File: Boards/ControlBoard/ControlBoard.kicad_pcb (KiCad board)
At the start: 4 copper layers, 250 x 150 mm, 181 parts, among them IC1 TXB0104DR, IC2 ADS8688AIDBT, IC3 ISO1042BDWVR, IC4 TXB0104DR, IC5 TXB0104DR, IC6 MCP2515-e_ST, IC7 TXB0104DR, IC8 TXB0104DR, J1 Conn_01x02_Pin, J10 5-106505-2, J11 5-106505-2, J12 5-106505-2, J13 5-106505-2, J14 5-106505-2, J15 1987724, J16 1987724, J17 1548129, J24 5442251, J3 1548129, J4 5-106505-2, J5 5442251, J6 L717SDB25PA4CH3R, J7 5442251, J8 5442251, J9 5442251, M1 Fan_4pin, M2 Fan_4pin, M3 Fan_4pin, M4 Fan_4pin, M5 Fan_4pin, M6 Fan_4pin, M7 Fan_4pin, M8 Fan_4pin, Y1 8MHz

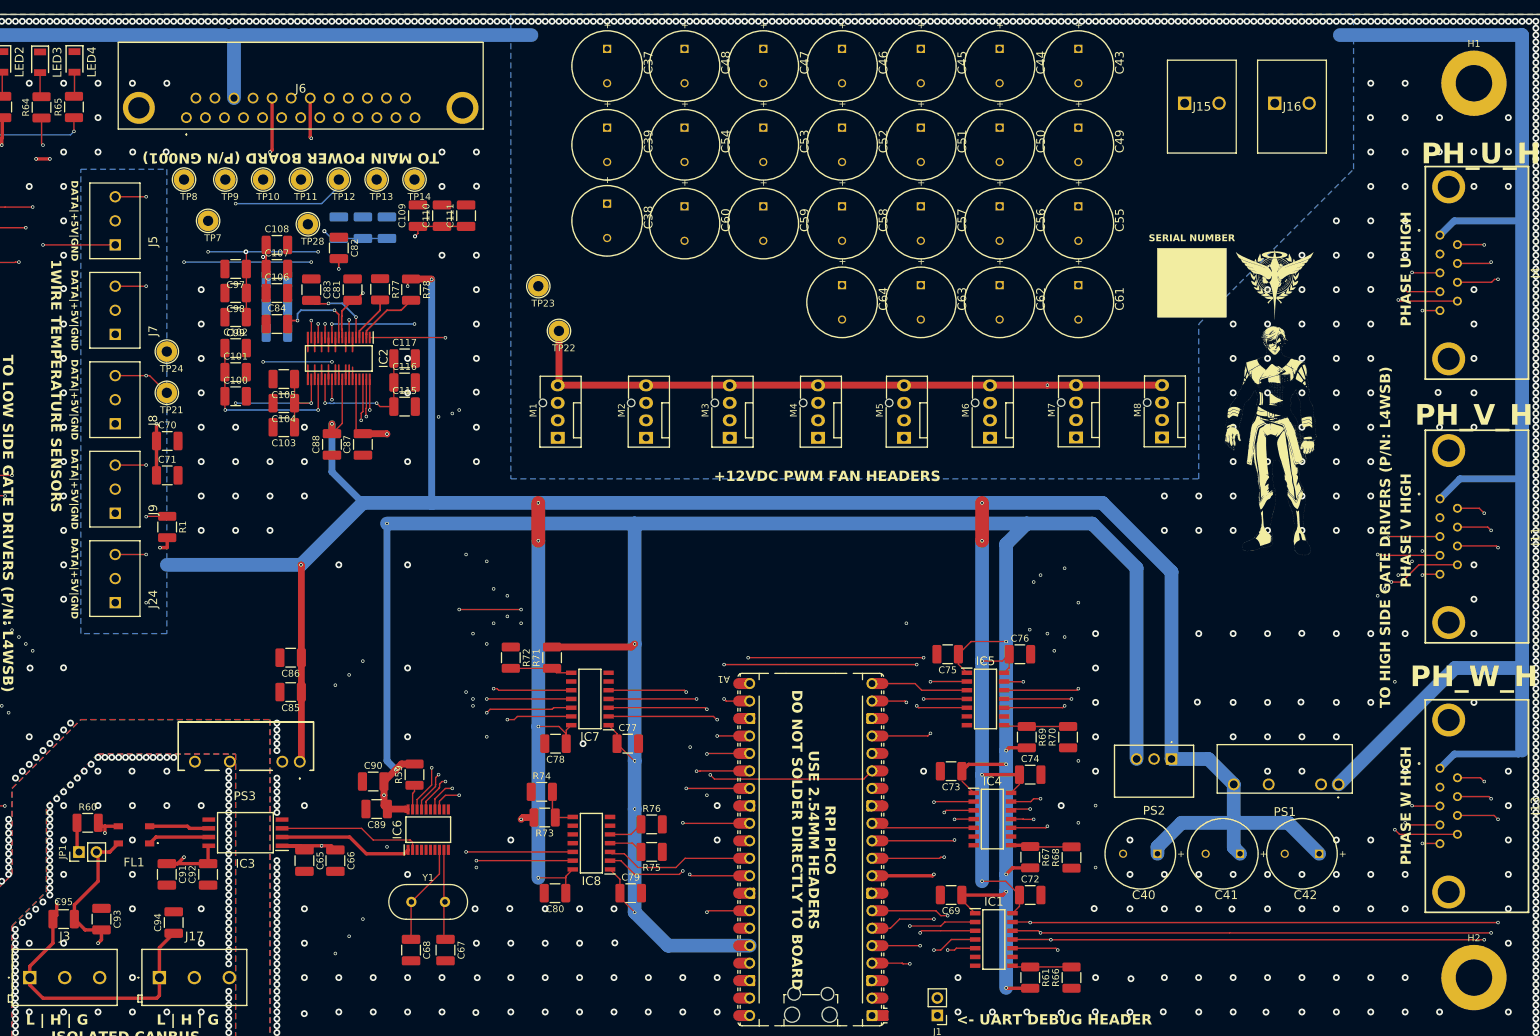
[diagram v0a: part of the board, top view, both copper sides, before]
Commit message: Update control board
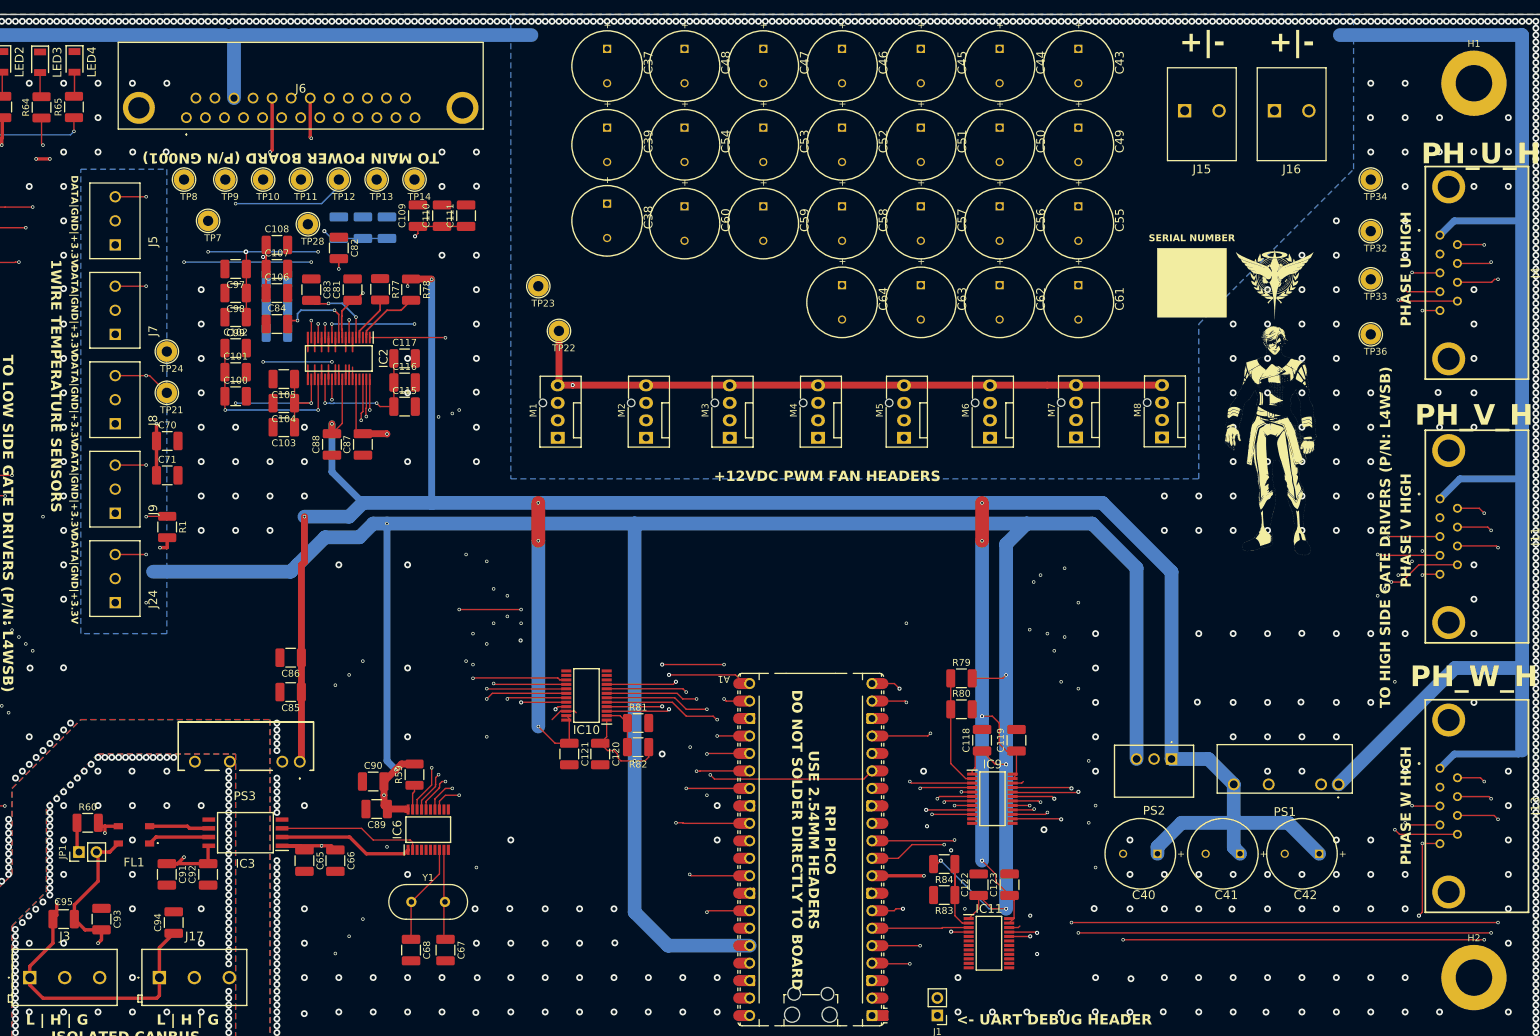
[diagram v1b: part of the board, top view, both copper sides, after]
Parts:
- removed C69, C72, C73, C74, C75, C76, C77, C78, C79, C80: 100nF, Capacitor_SMD:C_1210_3225Metric_Pad1.33x2.70mm_HandSolder
- removed IC1, IC4, IC5, IC7, IC8: TXB0104DR, InverterCom:SOIC127P600X175-14N
- removed R61, R66, R67, R68, R69, R70, R71, R72, R73, R74, R75, R76: 4.7k, Resistor_SMD:R_1210_3225Metric_Pad1.30x2.65mm_HandSolder
- removed REF**: OSHW-Logo2_14.6x12mm_SilkScreen, Symbol:OSHW-Logo2_14.6x12mm_SilkScreen
- removed REF**: ESD-Logo_13.2x12mm_SilkScreen, Symbol:ESD-Logo_13.2x12mm_SilkScreen
- removed REF**: KiCad-Logo2_8mm_SilkScreen, Symbol:KiCad-Logo2_8mm_SilkScreen
- removed REF**: WEEE-Logo_8.4x12mm_SilkScreen, Symbol:WEEE-Logo_8.4x12mm_SilkScreen
- added C118: 100nF, Capacitor_SMD:C_1210_3225Metric_Pad1.33x2.70mm_HandSolder, F.Cu at (193.5, 130.5)
- added C119: 100nF, Capacitor_SMD:C_1210_3225Metric_Pad1.33x2.70mm_HandSolder, F.Cu at (198.5, 130.5)
- added C120: 100nF, Capacitor_SMD:C_1210_3225Metric_Pad1.33x2.70mm_HandSolder, F.Cu at (138.0, 132.5)
- added C121: 100nF, Capacitor_SMD:C_1210_3225Metric_Pad1.33x2.70mm_HandSolder, F.Cu at (133.5, 132.5)
- added C122: 100nF, Capacitor_SMD:C_1210_3225Metric_Pad1.33x2.70mm_HandSolder, F.Cu at (193.0, 151.5)
- added C123: 100nF, Capacitor_SMD:C_1210_3225Metric_Pad1.33x2.70mm_HandSolder, F.Cu at (197.5, 151.5)
- added IC10: SN74LXCH8T245PWR, InverterCom:SOP65P640X120-24N, F.Cu at (136.0, 124.0)
- added IC11: SN74LXCH8T245PWR, InverterCom:SOP65P640X120-24N, F.Cu at (194.5, 160.0)
- added IC9: SN74LXCH8T245PWR, InverterCom:SOP65P640X120-24N, F.Cu at (195.0, 139.0)
- added R79: 4.7k, Resistor_SMD:R_1210_3225Metric_Pad1.30x2.65mm_HandSolder, F.Cu at (190.5, 121.5)
- added R80: 4.7k, Resistor_SMD:R_1210_3225Metric_Pad1.30x2.65mm_HandSolder, F.Cu at (190.5, 126.0)
- added R81: 4.7k, Resistor_SMD:R_1210_3225Metric_Pad1.30x2.65mm_HandSolder, F.Cu at (143.5, 128.0)
- added R82: 4.7k, Resistor_SMD:R_1210_3225Metric_Pad1.30x2.65mm_HandSolder, F.Cu at (143.5, 131.5)
- added R83: 4.7k, Resistor_SMD:R_1210_3225Metric_Pad1.30x2.65mm_HandSolder, F.Cu at (188.0, 153.0)
- added R84: 4.7k, Resistor_SMD:R_1210_3225Metric_Pad1.30x2.65mm_HandSolder, F.Cu at (188.0, 148.5)
- added TP32: TestPoint, TestPoint:TestPoint_Loop_D2.54mm_Drill1.5mm_Beaded, F.Cu at (250.0, 56.5)
- added TP33: TestPoint, TestPoint:TestPoint_Loop_D2.54mm_Drill1.5mm_Beaded, F.Cu at (250.0, 63.5)
- added TP34: TestPoint, TestPoint:TestPoint_Loop_D2.54mm_Drill1.5mm_Beaded, F.Cu at (250.0, 49.0)
- added TP36: TestPoint, TestPoint:TestPoint_Loop_D2.54mm_Drill1.5mm_Beaded, F.Cu at (250.0, 71.5)
- moved J16 1.10 mm to (236.0, 39.0)
- moved J15 1.10 mm to (222.9, 39.0)
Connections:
- C70 pad 1: +5V -> +3.3V
- C71 pad 1: +5V -> +3.3V
- J24 pad 1: +5V -> +3.3V
- J24 pad 3: 1WIRE_DATA -> 1WIRE_3v3_DATA
- J5 pad 1: +5V -> +3.3V
- J5 pad 3: 1WIRE_DATA -> 1WIRE_3v3_DATA
- J7 pad 1: +5V -> +3.3V
- J7 pad 3: 1WIRE_DATA -> 1WIRE_3v3_DATA
- J8 pad 1: +5V -> +3.3V
- J8 pad 3: 1WIRE_DATA -> 1WIRE_3v3_DATA
- J9 pad 1: +5V -> +3.3V
- J9 pad 3: 1WIRE_DATA -> 1WIRE_3v3_DATA
- R1 pad 1: 1WIRE_DATA -> 1WIRE_3v3_DATA
- R1 pad 2: +5V -> +3.3V
- TP21 pad 1: 1WIRE_DATA -> 1WIRE_3v3_DATA
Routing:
- net 1WIRE_3v3_DATA: track 13.4 -> 266.1 mm, vias 0 -> 10
- net 1WIRE_DATA: track 247.5 -> 0.00 mm, vias 9 -> 0
- net GATE_SPI_TX: track 482.1 -> 525.2 mm, vias 11 -> 12
- net GATE_SPI_SCK: track 486.0 -> 524.2 mm, vias 11 -> 12
- net FAULT_INPUT: track 479.7 -> 511.6 mm, vias 12 -> 14
- net FAULT_3v3_INPUT: track 21.0 -> 44.2 mm, vias 0 -> 2
- net GATE_U_L_CS: track 283.1 -> 260.4 mm
- net GATE_SPI_3v3_TX: track 16.3 -> 36.7 mm
- net GATE_SPI_3v3_SCK: track 20.8 -> 41.2 mm
- net GATE_SPI_RX: track 476.5 -> 496.0 mm, vias 11 -> 13
- net GATE_W_H_CS: track 87.7 -> 106.5 mm, vias 3 -> 4
- net PH_3v3_PWM_U_L: track 50.2 -> 32.0 mm
- net Net-(IC9-DIR): track 0.00 -> 16.4 mm
- net FAN_3v3_PWM: track 41.6 -> 25.6 mm, vias 3 -> 2
- net Net-(IC11-DIR): track 0.00 -> 14.5 mm
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- added copper zone on B.Cu, net +3.3V
- removed copper zone on B.Cu, net +5V
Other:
- board text added: "+|-"
- board text added: "DATA|GND|+3.3V"
- board text removed: "DATA|+5V|GND"
